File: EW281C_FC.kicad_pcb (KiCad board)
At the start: 4 copper layers, 29.5 x 29.5 mm, 87 parts, among them J10 Conn_01x08, J11 Conn_01x03, J12 Conn_01x02, J14 Conn_01x04, J2 Conn_01x04, J3 Conn_01x04, J4 Conn_01x03, J5 USB_B_Micro, J8 Conn_01x04, J9 Conn_01x08, Q1 BSS138, SW1 SW_Push, U1 LP2985-3.3, U10 W25Q128JVS, U2 STM32F722RETx, U3 LP2985-3.3, U5 MP4560_QFN10, U7 MPU-6000, U9 BMP388

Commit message: Changes made
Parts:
- removed C29: 2.2uF, Capacitor_SMD:C_0603_1608Metric
- removed J14, J3: Conn_01x04, Connector_Wire:Conn_4Pin
- removed J4: Conn_01x03, Connector_Wire:Conn_3Pin
- removed Q1: BSS138, Package_TO_SOT_SMD:SOT-23
- removed R1: 10k, Resistor_SMD:R_0402_1005Metric
- removed U9: BMP388, Footprints:BMP388
- added C12: 0.1uF, Capacitor_SMD:C_0402_1005Metric, B.Cu at (92.0, 101.9)
- added J1: Conn_01x03, Connector_JST:JST_SH_SM03B-SRSS-TB_1x03-1MP_P1.00mm_Horizontal, F.Cu at (95.8, 108.2)
- added U4: BMP280, Package_LGA:Bosch_LGA-8_2x2.5mm_P0.65mm_ClockwisePinNumbering, F.Cu at (84.4, 90.2)
- C30: value 2.2uF -> 4.7uF
- C36: value 2pF -> 1pF
- J11: footprint Connector_Wire:Conn_3Pin -> Connector_JST:JST_SH_SM03B-SRSS-TB_1x03-1MP_P1.00mm_Horizontal; moved to B.Cu
- L2: value 12uH -> 15uH
- R19: value 200k -> 195k
- R24: value 68k -> 88.7k
- U5: value MP4560_QFN10 -> MP4561_QFN10
- moved J2 3.50 mm to (87.8, 110.4)
- moved L4 1.58 mm to (89.7, 102.5)
- moved C30 1.46 mm to (93.2, 101.3)
- moved R3 0.81 mm to (103.0, 103.2)
- moved R4 0.81 mm to (103.0, 102.2)
- moved J12 0.81 mm to (104.9, 102.7)
- moved L3 0.80 mm to (87.2, 103.2)
- moved R19 0.52 mm to (91.1, 101.9)
- moved J8 0.50 mm to (78.3, 93.8)
- moved J11 0.21 mm to (79.8, 102.2), turned to 90 degrees
- moved C10 0.19 mm to (84.2, 88.5), turned to 180 degrees
- moved C9 0.19 mm to (86.0, 88.5), turned to 180 degrees
- moved J10 0.07 mm to (104.9, 94.8)
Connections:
- U2 pad 16: /Connectors/UART2_TX -> (no net)
- U2 pad 24: /MCU/BUZ-_MCU -> (no net)
- U2 pad 37: /Connectors/UART6_TX -> (no net)
- U5 pad 8: VCC -> Net-(C12-Pad2)
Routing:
- net /Connectors/UART6_RX: track 56.9 -> 30.2 mm, vias 6 -> 4
- net /Connectors/UART6_TX: track 20.3 -> 0.00 mm, vias 1 -> 0
- net /Connectors/UART2_TX: track 15.9 -> 0.00 mm
- net +5V: track 71.1 -> 57.4 mm, vias 2 -> 4
- net 4V5: track 29.6 -> 17.4 mm, vias 3 -> 2
- net /MCU/BUZ-_MCU: track 8.82 -> 0.00 mm, vias 1 -> 0
- net /Connectors/UART2_RX: track 16.1 -> 8.30 mm, vias 0 -> 1
- net /Connectors/BUZ-: track 6.29 -> 0.00 mm
- net +3V3: track 38.7 -> 42.8 mm, vias 11 -> 13
- net VCC: track 33.5 -> 37.0 mm
- net /Connectors/LED: track 20.2 -> 16.9 mm
- net /Connectors/I2C1_SCL: track 27.9 -> 30.7 mm
- net /Connectors/UART3_TX: track 15.2 -> 13.4 mm
- net /Connectors/I2C1_SDA: track 28.2 -> 29.9 mm
- net /Connectors/UART3_RX: track 14.2 -> 12.7 mm
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- removed copper zone on B.Cu, net VCC
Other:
- board text added: "RX2"
- board text added: "RX3"
- board text added: "SCL"
- board text added: "SDA"
- board text added: "TX3"
- board text removed: "4V5"
- board text removed: "BUZ"

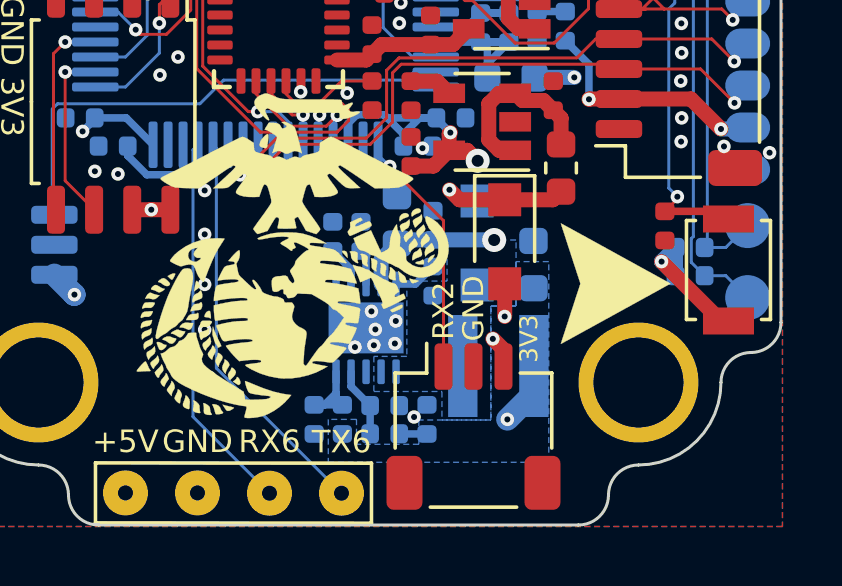
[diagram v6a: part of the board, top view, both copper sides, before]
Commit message: Changed some components to match what is in stock
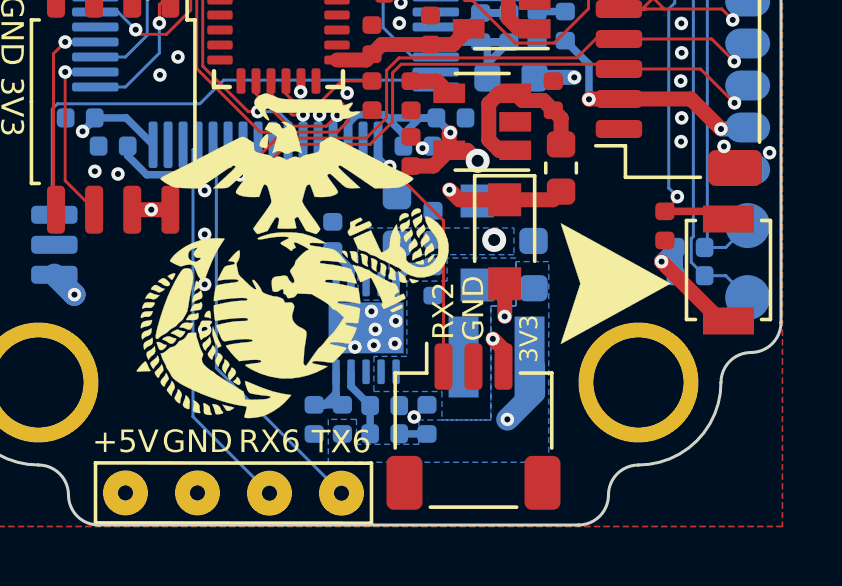
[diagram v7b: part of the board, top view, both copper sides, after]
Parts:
- removed C12: 0.1uF, Capacitor_SMD:C_0402_1005Metric
- C34: value 560pF -> 820pF
- C36: value 1pF -> 2pF
- D9: value PURPLE -> GREEN
- L2: footprint Inductor_SMD:L_XGL4030 -> Inductor_SMD:L_Bourns-SRN3015
- R19: value 195k -> 200k
- R24: value 88.7k -> 56k
- R26: value 100 -> 1k
- U5: value MP4561_QFN10 -> MP4462
- moved L2 0.31 mm to (96.5, 105.9), turned to 270 degrees
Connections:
- U5 pad 8: Net-(C12-Pad2) -> VCC
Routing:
- net VCC: track 37.0 -> 32.1 mm
- net Net-(C12-Pad2): track 1.17 -> 0.00 mm
- added copper zone on B.Cu, net VCC
